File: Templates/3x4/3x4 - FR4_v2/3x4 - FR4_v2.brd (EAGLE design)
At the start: 108.6 x 83.2 mm, 1 part

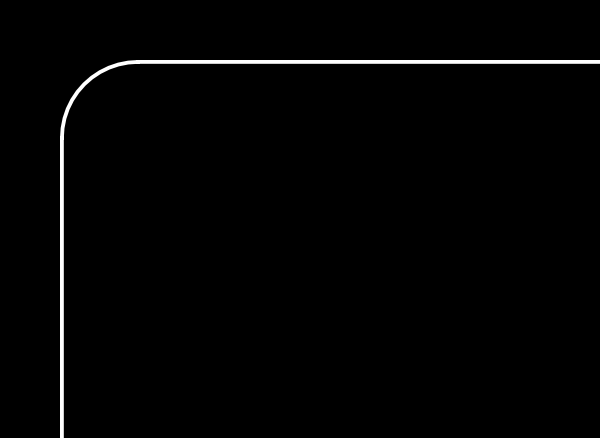
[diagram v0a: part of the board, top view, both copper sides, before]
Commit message: Updated 4x5 to make fiducial a bit smaller to meet our bounds. Added 'fr4' silkscreen to 2x3, 3x4 and 4x5 substrates
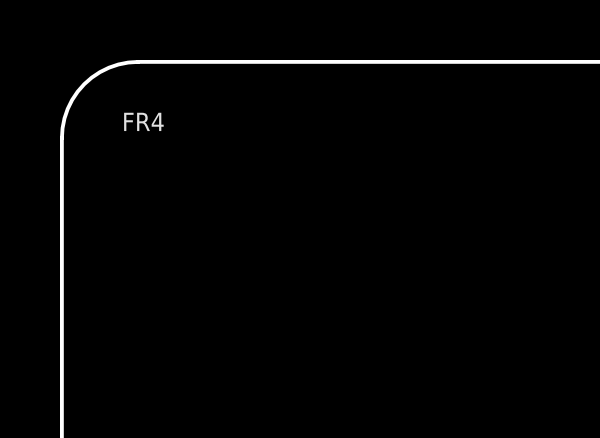
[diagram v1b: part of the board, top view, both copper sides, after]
